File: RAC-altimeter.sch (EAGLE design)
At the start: 25 parts, among them J1 MICRO-SD, U1 MAX32660GTP+, U2 BMI088, U3 BMP388, U4 RN4871-I_RM130, U5 TPS62172DSGR, Y1 32.768kHz

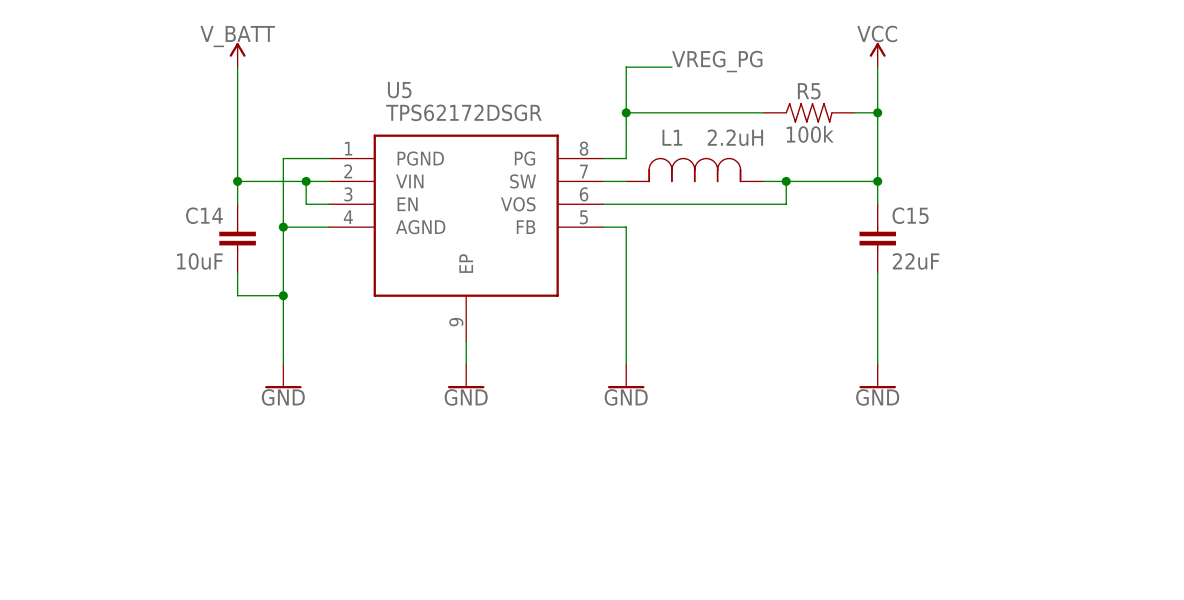
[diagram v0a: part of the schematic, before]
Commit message: Replaced the buck converter with the MCP1640 boost converter
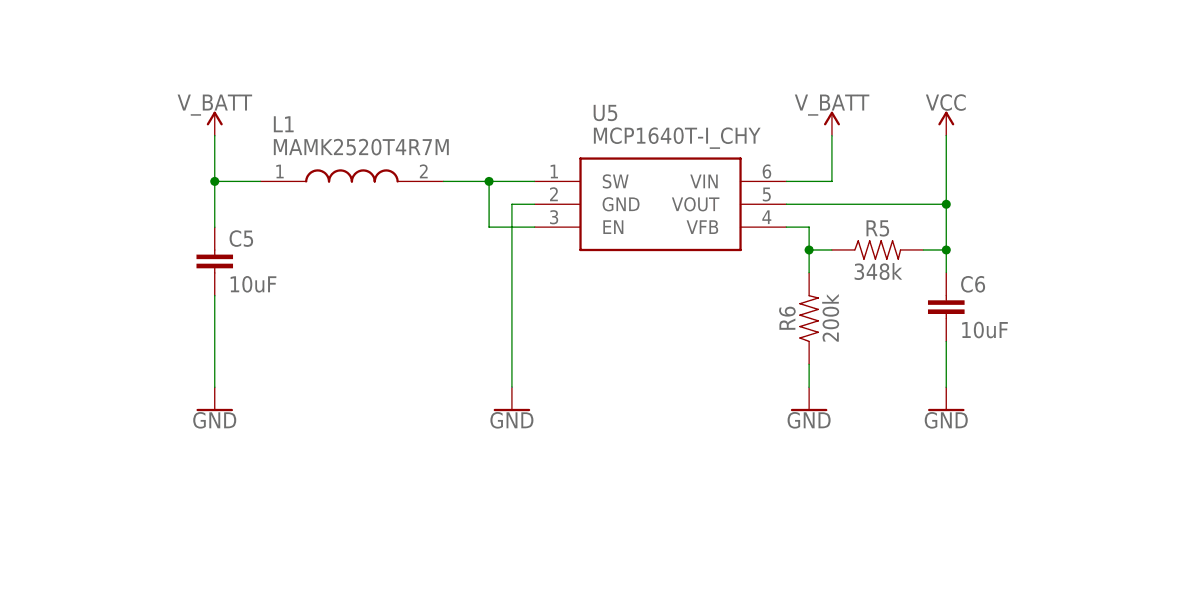
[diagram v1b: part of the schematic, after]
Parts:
- removed C14: 10uF, SparkFun-Capacitors:10UF-0603-6.3V-20%
- removed C15: 22uF, SparkFun-Capacitors:22UF-0805-6.3V-20%
- added C5, C6: 10uF, SparkFun-Capacitors:10UF-0603-6.3V-20%
- added R6: 200k, SparkFun-Resistors:200KOHM-0603-1/10W-1%
- L1: value 2.2uH -> MAMK2520T4R7M; device RAC-Altimeter:MAMK2520T2R2M -> RAC-Altimeter:MAMK2520T4R7M
- R5: value 100k -> 348k; device SparkFun-Resistors:100KOHM-0603-1/10W-1% -> SparkFun-Resistors:348KOHM-0603-1/10W-1%
- U5: value TPS62172DSGR -> MCP1640T-I_CHY; device RAC-Altimeter:TPS62172DSGR -> RAC-Altimeter:MCP1640T-I_CHY
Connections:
- removed net N$1: L1.2, U5.SW
- removed net VREG_PG: R5.1, U5.PG
- new net N$2: L1.2, U5.EN, U5.SW
- new net N$3: R5.1, R6.2, U5.VFB
- net GND: now also C5.2, C6.2, R6.1, U5.GND; no longer C14.2, C15.2, U5.AGND, U5.EP, U5.FB, U5.PGND
- net VCC: now also C6.1, U5.VOUT; no longer C15.1, L1.1, U5.VOS
- net V_BATT: now also C5.1, L1.1; no longer C14.1, U5.EN
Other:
- moved on the sheet: R5

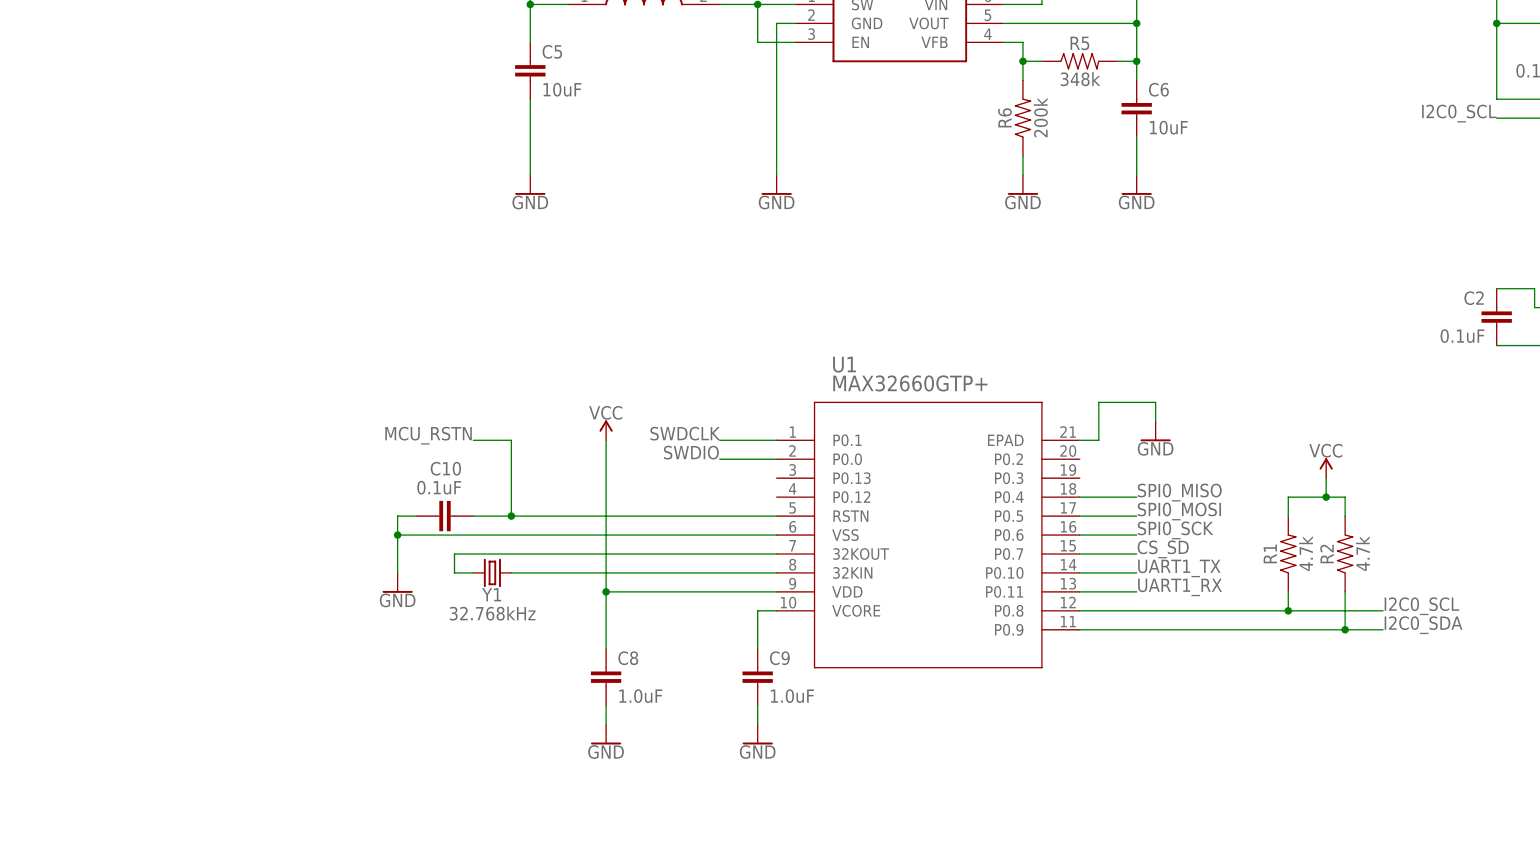
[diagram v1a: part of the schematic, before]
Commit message: Added SWD 10-pin header, battery terminals, and GPIO LED
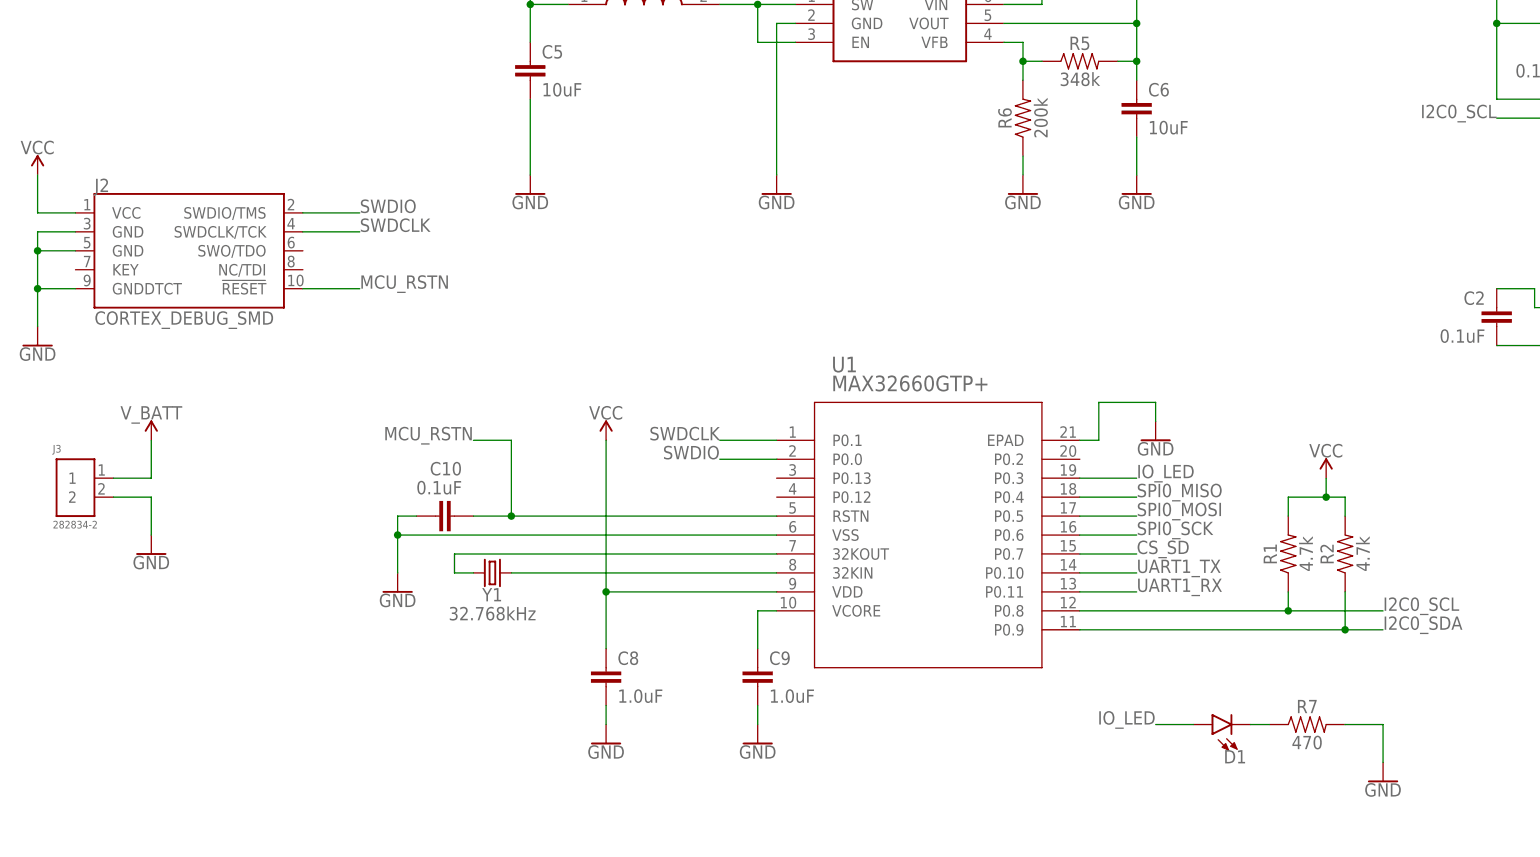
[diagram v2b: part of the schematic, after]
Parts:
- added D1: (no value), SparkFun-LED:LED0603
- added J2: CORTEX_DEBUG_SMD, SparkFun-Connectors:CORTEX_DEBUG_SMD
- added J3: 282834-2, RAC-Altimeter:282834-2
- added R7: 470, SparkFun-Resistors:470OHM-0603-1/10W-1%
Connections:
- new net IO_LED: D1.A, U1.P0.3
- new net LED_CATH: D1.C, R7.1
- net GND: now also J2.GND@3, J2.GND@5, J2.GNDDTCT, J3.2, R7.2
- net MCU_RSTN: now also J2.!RESET
- net SWDCLK: now also J2.SWDCLK/TCK
- net SWDIO: now also J2.SWDIO/TMS
- net VCC: now also J2.VCC
- net V_BATT: now also J3.1
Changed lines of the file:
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@@
 <part name="GND13" library="SparkFun-PowerSymbols" deviceset="GND" device=""/>
 <part name="GND14" library="SparkFun-PowerSymbols" deviceset="GND" device=""/>
+<part name="D1" library="SparkFun-LED" library_urn="urn:adsk.eagle:library:529" deviceset="LED" device="0603" package3d_urn="urn:adsk.eagle:package:39354/1"/>
+<part name="R7" library="SparkFun-Resistors" library_urn="urn:adsk.eagle:library:532" deviceset="470OHM" device="-0603-1/10W-1%" package3d_urn="urn:adsk.eagle:package:39650/1" value="470"/>
+<part name="GND8" library="SparkFun-PowerSymbols" deviceset="GND" device=""/>
+<part name="J2" library="SparkFun-Connectors" deviceset="CORTEX_DEBUG" device="_SMD"/>
+<part name="GND11" library="SparkFun-PowerSymbols" deviceset="GND" device=""/>
+<part name="SUPPLY11" library="SparkFun-PowerSymbols" deviceset="VCC" device=""/>
+<part name="J3" library="RAC-Altimeter" deviceset="282834-2" device=""/>
+<part name="SUPPLY12" library="SparkFun-PowerSymbols" deviceset="V_BATT" device=""/>
+<part name="GND15" library="SparkFun-PowerSymbols" deviceset="GND" device=""/>
 </parts>
 <sheets>
@@
 <instance part="GND14" gate="1" x="63.5" y="93.98" smashed="yes">
 <attribute name="VALUE" x="63.5" y="93.726" size="1.778" layer="96" align="top-center"/>
+</instance>
+<instance part="D1" gate="G$1" x="73.66" y="22.86" smashed="yes" rot="R90">
+<attribute name="NAME" x="78.232" y="19.431" size="1.778" layer="95" font="vector" rot="R180"/>
+<attribute name="VALUE" x="78.232" y="24.765" size="1.778" layer="96" font="vector" rot="R180" align="top-left"/>
+</instance>
+<instance part="R7" gate="G$1" x="86.36" y="22.86" smashed="yes">
+<attribute name="NAME" x="86.36" y="24.384" size="1.778" layer="95" font="vector" align="bottom-center"/>
+<attribute name="VALUE" x="86.36" y="21.336" size="1.778" layer="96" font="vector" align="top-center"/>
+</instance>
+<instance part="GND8" gate="1" x="96.52" y="15.24" smashed="yes">
+<attribute name="VALUE" x="96.52" y="14.986" size="1.778" layer="96" align="top-center"/>
+</instance>
+<instance part="J2" gate="J1" x="-63.5" y="86.36" smashed="yes">
+<attribute name="NAME" x="-76.2" y="94.234" size="1.778" layer="95" font="vector"/>
+<attribute name="VALUE" x="-76.2" y="76.454" size="1.778" layer="96" font="vector"/>
+</instance>
+<instance part="GND11" gate="1" x="-83.82" y="73.66" smashed="yes">
+<attribute name="VALUE" x="-83.82" y="73.406" size="1.778" layer="96" align="top-center"/>
+</instance>
+<instance part="SUPPLY11" gate="G$1" x="-83.82" y="96.52" smashed="yes">
+<attribute name="VALUE" x="-83.82" y="99.314" size="1.778" layer="96" align="bottom-center"/>
+</instance>
+<instance part="J3" gate="G$1" x="-78.74" y="55.88" smashed="yes">
+<attribute name="NAME" x="-81.79226875" y="59.313809375" size="1.01741875" layer="95"/>
+<attribute name="VALUE" x="-81.79121875" y="49.1419" size="1.01706875" layer="96"/>
+</instance>
+<instance part="SUPPLY12" gate="G$1" x="-68.58" y="60.96" smashed="yes">
+<attribute name="VALUE" x="-68.58" y="63.754" size="1.778" layer="96" align="bottom-center"/>
+</instance>
+<instance part="GND15" gate="1" x="-68.58" y="45.72" smashed="yes">
+<attribute name="VALUE" x="-68.58" y="45.466" size="1.778" layer="96" align="top-center"/>
 </instance>
 </instances>
@@
 <wire x1="63.5" y1="101.6" x2="63.5" y2="96.52" width="0.1524" layer="91"/>
 </segment>
+<segment>
+<pinref part="R7" gate="G$1" pin="2"/>
+<pinref part="GND8" gate="1" pin="GND"/>
+<wire x1="91.44" y1="22.86" x2="96.52" y2="22.86" width="0.1524" layer="91"/>
+<wire x1="96.52" y1="22.86" x2="96.52" y2="17.78" width="0.1524" layer="91"/>
+</segment>
+<segment>
+<pinref part="J2" gate="J1" pin="GNDDTCT"/>
+<wire x1="-78.74" y1="81.28" x2="-83.82" y2="81.28" width="0.1524" layer="91"/>
+<pinref part="GND11" gate="1" pin="GND"/>
+<wire x1="-83.82" y1="81.28" x2="-83.82" y2="76.2" width="0.1524" layer="91"/>
+<pinref part="J2" gate="J1" pin="GND@5"/>
+<wire x1="-78.74" y1="86.36" x2="-83.82" y2="86.36" width="0.1524" layer="91"/>
+<wire x1="-83.82" y1="86.36" x2="-83.82" y2="81.28" width="0.1524" layer="91"/>
+<junction x="-83.82" y="81.28"/>
+<pinref part="J2" gate="J1" pin="GND@3"/>
+<wire x1="-78.74" y1="88.9" x2="-83.82" y2="88.9" width="0.1524" layer="91"/>
+<wire x1="-83.82" y1="88.9" x2="-83.82" y2="86.36" width="0.1524" layer="91"/>
+<junction x="-83.82" y="86.36"/>
+</segment>
+<segment>
+<pinref part="J3" gate="G$1" pin="2"/>
+<wire x1="-73.66" y1="53.34" x2="-68.58" y2="53.34" width="0.1524" layer="91"/>
+<wire x1="-68.58" y1="53.34" x2="-68.58" y2="48.26" width="0.1524" layer="91"/>
+<pinref part="GND15" gate="1" pin="GND"/>
+</segment>
 </net>
 <net name="I2C0_SCL" class="0">
@@
 <junction x="63.5" y="111.76"/>
 </segment>
+<segment>
+<pinref part="J2" gate="J1" pin="VCC"/>
+<wire x1="-78.74" y1="91.44" x2="-83.82" y2="91.44" width="0.1524" layer="91"/>
+<pinref part="SUPPLY11" gate="G$1" pin="VCC"/>
+<wire x1="-83.82" y1="91.44" x2="-83.82" y2="96.52" width="0.1524" layer="91"/>
+</segment>
 </net>
 <net name="N$5" class="0">
@@
 <label x="-25.4" y="60.96" size="1.778" layer="95" rot="MR0"/>
 </segment>
+<segment>
+<pinref part="J2" gate="J1" pin="!RESET"/>
+<wire x1="-48.26" y1="81.28" x2="-40.64" y2="81.28" width="0.1524" layer="91"/>
+<label x="-40.64" y="81.28" size="1.778" layer="95"/>
+</segment>
 </net>
 <net name="SWDIO" class="0">
@@
 <label x="7.62" y="58.42" size="1.778" layer="95" rot="MR0"/>
 </segment>
+<segment>
+<pinref part="J2" gate="J1" pin="SWDIO/TMS"/>
+<wire x1="-48.26" y1="91.44" x2="-40.64" y2="91.44" width="0.1524" layer="91"/>
+<label x="-40.64" y="91.44" size="1.778" layer="95"/>
+</segment>
 </net>
 <net name="SWDCLK" class="0">
@@
 <wire x1="15.24" y1="60.96" x2="7.62" y2="60.96" width="0.1524" layer="91"/>
 <label x="7.62" y="60.96" size="1.778" layer="95" rot="MR0"/>
+</segment>
+<segment>
+<pinref part="J2" gate="J1" pin="SWDCLK/TCK"/>
+<wire x1="-48.26" y1="88.9" x2="-40.64" y2="88.9" width="0.1524" layer="91"/>
+<label x="-40.64" y="88.9" size="1.778" layer="95"/>
 </segment>
 </net>
@@
 <pinref part="U5" gate="G$1" pin="VIN"/>
 <wire x1="50.8" y1="119.38" x2="45.72" y2="119.38" width="0.1524" layer="91"/>
+</segment>
+<segment>
+<pinref part="J3" gate="G$1" pin="1"/>
+<wire x1="-73.66" y1="55.88" x2="-68.58" y2="55.88" width="0.1524" layer="91"/>
+<wire x1="-68.58" y1="55.88" x2="-68.58" y2="60.96" width="0.1524" layer="91"/>
+<pinref part="SUPPLY12" gate="G$1" pin="V_BATT"/>
 </segment>
 </net>
@@
 </segment>
 </net>
+<net name="IO_LED" class="0">
+<segment>
+<pinref part="U1" gate="A" pin="P0.3"/>
+<wire x1="55.88" y1="55.88" x2="63.5" y2="55.88" width="0.1524" layer="91"/>
+<label x="63.5" y="55.88" size="1.778" layer="95"/>
+</segment>
+<segment>
+<pinref part="D1" gate="G$1" pin="A"/>
+<wire x1="71.12" y1="22.86" x2="66.04" y2="22.86" width="0.1524" layer="91"/>
+<label x="66.04" y="22.86" size="1.778" layer="95" rot="MR0"/>
+</segment>
+</net>
+<net name="LED_CATH" class="0">
+<segment>
+<pinref part="R7" gate="G$1" pin="1"/>
+<pinref part="D1" gate="G$1" pin="C"/>
+<wire x1="81.28" y1="22.86" x2="78.74" y2="22.86" width="0.1524" layer="91"/>
+</segment>
+</net>

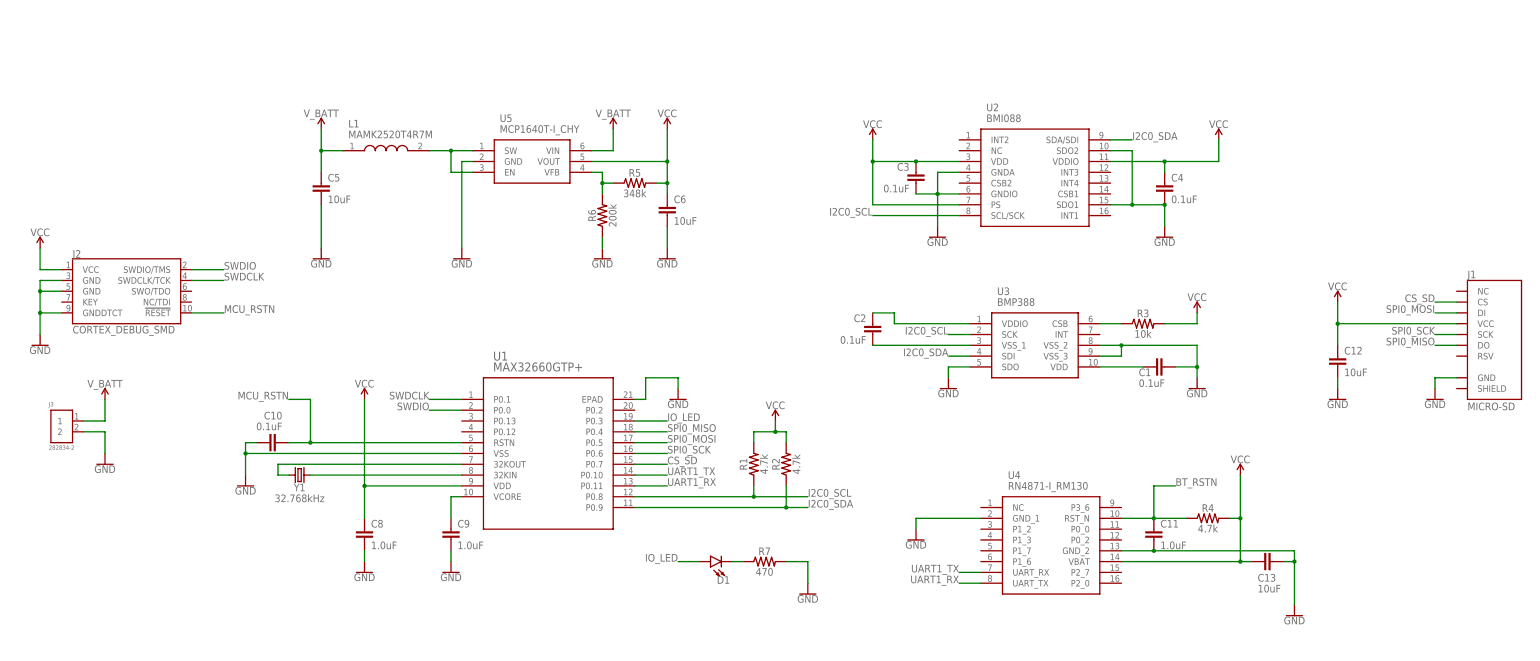
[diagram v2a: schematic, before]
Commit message: Added reset button, power enable switch, and power enable jumper
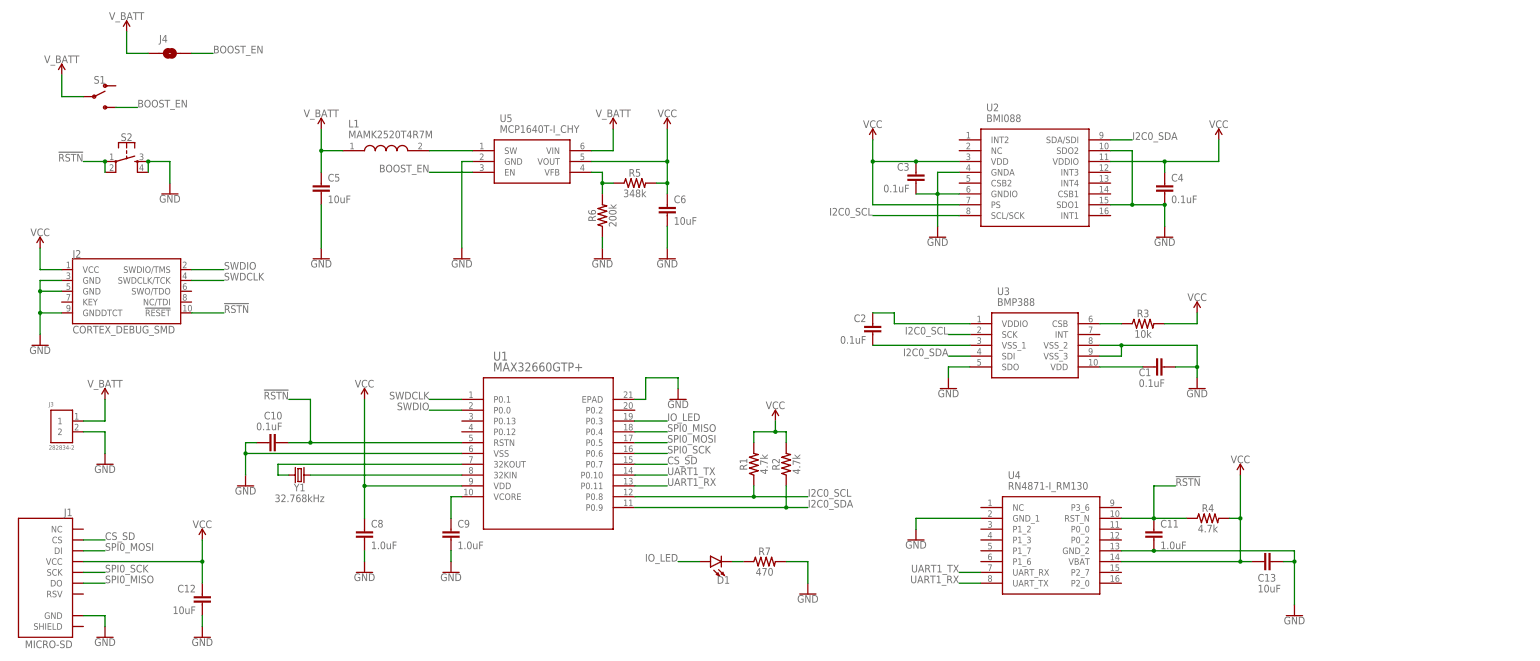
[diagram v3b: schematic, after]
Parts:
- added J4: JUMPER-SMT_2_NO_SILK, SparkFun-Jumpers:JUMPER-SMT_2_NO_SILK
- added S1: (no value), SparkFun-Switches:SWITCH-SPDT-SMD-AYZ0202
- added S2: (no value), SparkFun-Switches:MOMENTARY-SWITCH-SPST-2-SMD-4.6X2.8MM
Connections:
- removed net BT_RSTN: C11.1, R4.1, U4.RST_N
- removed net MCU_RSTN: C10.1, J2.!RESET, U1.RSTN
- new net !RSTN: C10.1, C11.1, J2.!RESET, R4.1, S2.1, S2.2, U1.RSTN, U4.RST_N
- new net BOOST_EN: J4.2, S1.S, U5.EN
- net GND: now also S2.3, S2.4
- net N$2: no longer U5.EN
- net V_BATT: now also J4.1, S1.P
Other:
- moved on the sheet: C12, J1
